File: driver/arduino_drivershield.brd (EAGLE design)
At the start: 59.7 x 54.3 mm, 24 parts, among them IC1 LB1973M, IC10 LB1973M, IC11 LB1973M, IC12 74HC14D, IC2 LB1973M, IC3 74HC14D, IC4 LB1973M, IC5 LB1973M, IC6 74HC14D, IC7 LB1973M, IC8 LB1973M, IC9 74HC14D, J1 J5MM, J2 J5MM, U1 ARDUINO_SHIELDLABEL

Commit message: testing routing
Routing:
- net @GND2: track 0.00 -> 157.7 mm, vias 0 -> 1
- net 5V: track 0.00 -> 111.5 mm, vias 0 -> 1
- net V+: track 0.00 -> 96.8 mm, vias 0 -> 2
- net GNDA: track 0.00 -> 92.5 mm, vias 0 -> 1
- net N$28: track 0.00 -> 90.5 mm
- net N$51: track 0.00 -> 74.4 mm, vias 0 -> 2
- net N$70: track 0.00 -> 32.1 mm
- net TX: track 0.00 -> 29.6 mm
- net RX: track 0.00 -> 29.0 mm
- net N$30: track 0.00 -> 25.0 mm, vias 0 -> 1
- net N$15: track 0.00 -> 23.9 mm, vias 0 -> 1
- net N$16: track 0.00 -> 23.9 mm, vias 0 -> 1
- net N$66: track 0.00 -> 23.5 mm, vias 0 -> 1
- net N$36: track 0.00 -> 22.2 mm, vias 0 -> 1
- net N$35: track 0.00 -> 21.8 mm
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
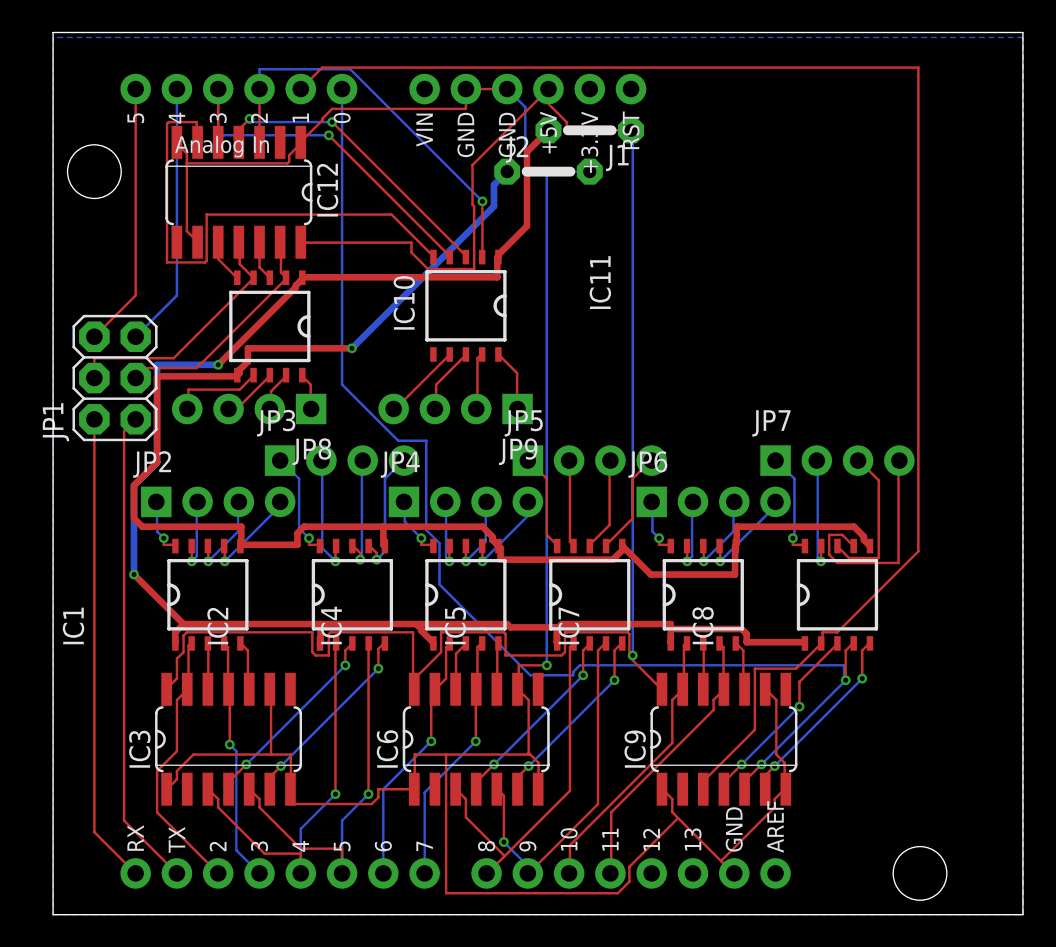
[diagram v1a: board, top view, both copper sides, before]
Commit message: bypass caps for all h-bridges
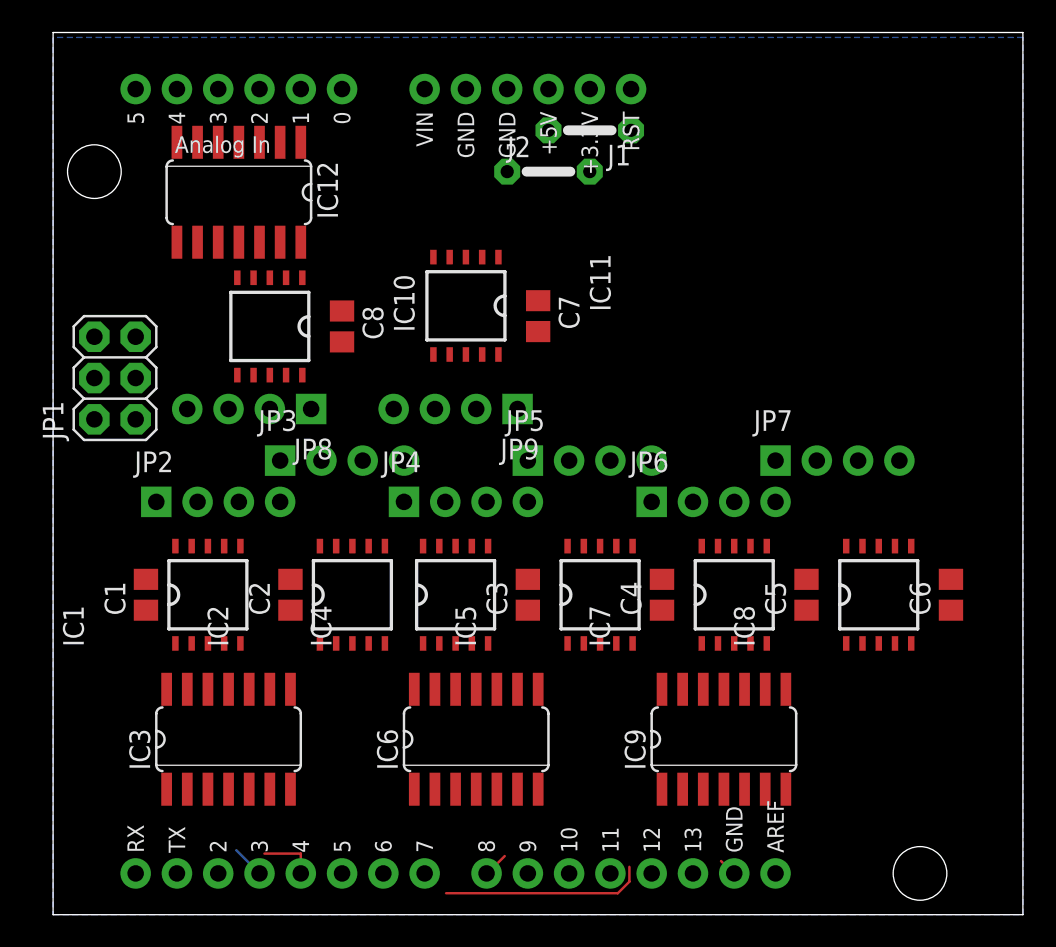
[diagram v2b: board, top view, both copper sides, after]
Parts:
- added C1, C2, C3, C4, C5, C6, C7, C8: (no value), rcl:C0805
- moved IC8 2.54 mm to (50.8, 19.7)
- moved IC7 1.90 mm to (41.9, 19.7)
- moved IC4 0.63 mm to (24.8, 19.7)
- moved IC5 0.63 mm to (33.7, 19.7)
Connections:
- net GNDA: now also C1.2, C2.2, C3.2, C4.2, C5.2, C6.2, C7.2, C8.2
- net V+: now also C1.1, C2.1, C3.1, C4.1, C5.1, C6.1, C7.1, C8.1
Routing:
- net @GND2: track 157.7 -> 13.6 mm, vias 1 -> 0
- net 5V: track 111.5 -> 0.00 mm, vias 1 -> 0
- net V+: track 96.8 -> 0.00 mm, vias 2 -> 0
- net GNDA: track 92.5 -> 0.00 mm, vias 1 -> 0
- net N$28: track 90.5 -> 0.00 mm
- net N$51: track 74.4 -> 0.00 mm, vias 2 -> 0
- net N$70: track 32.1 -> 0.00 mm
- net TX: track 29.6 -> 0.00 mm
- net RX: track 29.0 -> 0.00 mm
- net N$30: track 25.0 -> 0.00 mm, vias 1 -> 0
- net N$16: track 23.9 -> 0.00 mm, vias 1 -> 0
- net N$66: track 23.5 -> 0.00 mm, vias 1 -> 0
- net N$36: track 22.2 -> 0.61 mm, vias 1 -> 0
- net N$15: track 23.9 -> 3.45 mm, vias 1 -> 0
- net N$35: track 21.8 -> 1.56 mm
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
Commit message: the expiriment with the @signal names did not work out
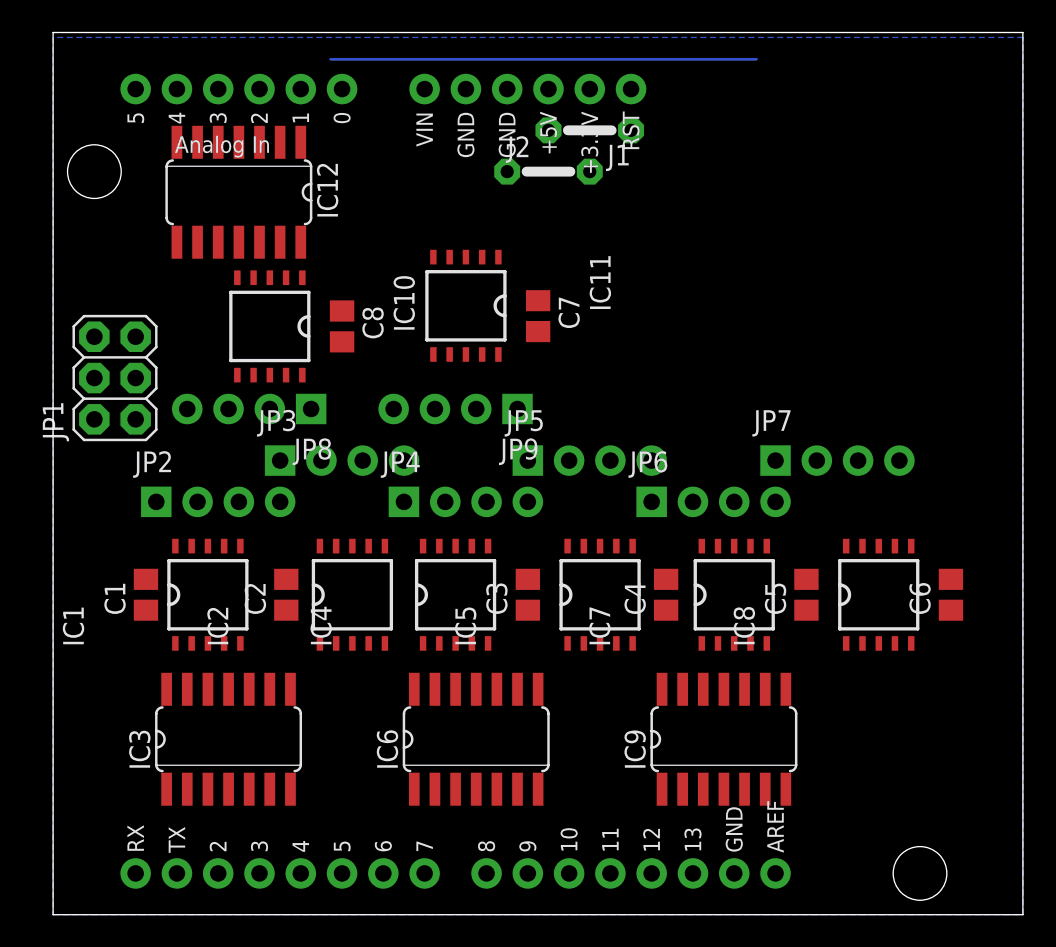
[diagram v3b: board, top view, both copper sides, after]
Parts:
- moved C2 0.25 mm to (14.4, 19.7)
- moved C4 0.25 mm to (37.7, 19.7)
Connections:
- removed net @GND3: IC11.6
- net GNDA: now also IC11.6
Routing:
- net N$28: track 0.00 -> 26.2 mm
- net @GND2: track 13.6 -> 0.00 mm
- net N$15: track 3.45 -> 0.00 mm
- net N$13: track 2.01 -> 0.00 mm
- net N$35: track 1.56 -> 0.00 mm
- net N$36: track 0.61 -> 0.00 mm

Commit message: the expiriment with the @signal names did not work out
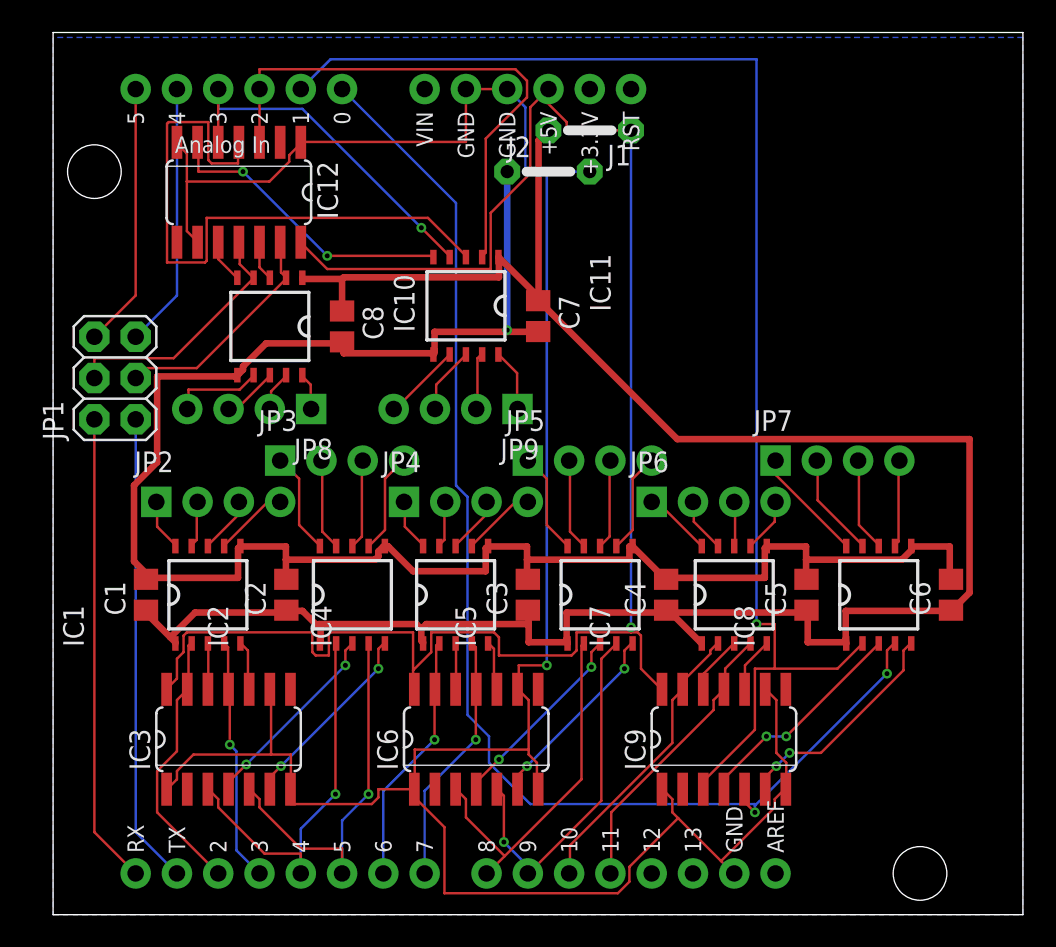
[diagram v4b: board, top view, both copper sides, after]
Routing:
- net @GND2: track 0.00 -> 158.4 mm, vias 0 -> 1
- net V+: track 0.00 -> 136.6 mm
- net GNDA: track 0.00 -> 116.1 mm, vias 0 -> 1
- net 5V: track 0.00 -> 109.4 mm, vias 0 -> 1
- net N$51: track 0.00 -> 78.4 mm, vias 0 -> 2
- net N$28: track 26.2 -> 83.4 mm, vias 0 -> 1
- net N$69: track 0.00 -> 38.8 mm
- net N$30: track 0.00 -> 33.2 mm
- net TX: track 0.00 -> 29.0 mm
- net RX: track 0.00 -> 29.0 mm
- net N$15: track 0.00 -> 23.9 mm, vias 0 -> 1
- net N$16: track 0.00 -> 23.9 mm, vias 0 -> 1
- net N$66: track 0.00 -> 22.5 mm, vias 0 -> 1
- net N$36: track 0.00 -> 22.4 mm, vias 0 -> 1
- net N$35: track 0.00 -> 22.0 mm
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
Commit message: the formar was SIGNAL@num...
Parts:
- removed J2: J5MM, jumper:05
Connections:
- net 5V renamed 5V@1
- removed net @GND2: IC12.1, IC12.7, IC12.9, IC3.1, IC3.7, IC3.9, IC6.1, IC6.7, IC6.9, IC9.1, IC9.7, IC9.9, J2.2, U1.GND@0, U1.GND@1, U1.GND@2
- removed net GNDA: C1.2, C2.2, C3.2, C4.2, C5.2, C6.2, C7.2, C8.2, IC1.6, IC10.6, IC11.6, IC2.6, IC4.6, IC5.6, IC7.6, IC8.6, J2.1
- new net GND@2: IC12.1, IC12.7, IC12.9, IC3.1, IC3.7, IC3.9, IC6.1, IC6.7, IC6.9, IC9.1, IC9.7, IC9.9, U1.GND@0, U1.GND@1, U1.GND@2
- new net GND@3: C1.2, C2.2, C3.2, C4.2, C5.2, C6.2, C7.2, C8.2, IC1.6, IC10.6, IC11.6, IC2.6, IC4.6, IC5.6, IC7.6, IC8.6
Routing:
- net @GND2: track 158.4 -> 0.00 mm, vias 1 -> 0
- net V+: track 136.6 -> 0.00 mm
- net GNDA: track 116.1 -> 0.00 mm, vias 1 -> 0
- net 5V@1: track 109.4 -> 0.00 mm, vias 1 -> 0
- net N$28: track 83.4 -> 0.00 mm, vias 1 -> 0
- net N$51: track 78.4 -> 0.00 mm, vias 2 -> 0
- net N$69: track 38.8 -> 0.00 mm
- net N$30: track 33.2 -> 0.00 mm
- net TX: track 29.0 -> 0.00 mm
- net RX: track 29.0 -> 0.00 mm
- net N$15: track 23.9 -> 0.00 mm, vias 1 -> 0
- net N$16: track 23.9 -> 0.00 mm, vias 1 -> 0
- net N$66: track 22.5 -> 0.00 mm, vias 1 -> 0
- net N$36: track 22.4 -> 0.00 mm, vias 1 -> 0
- net N$35: track 22.0 -> 0.00 mm
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- added copper zone on layer 16, net GND@2
- removed copper zone on layer 16, net @GND1

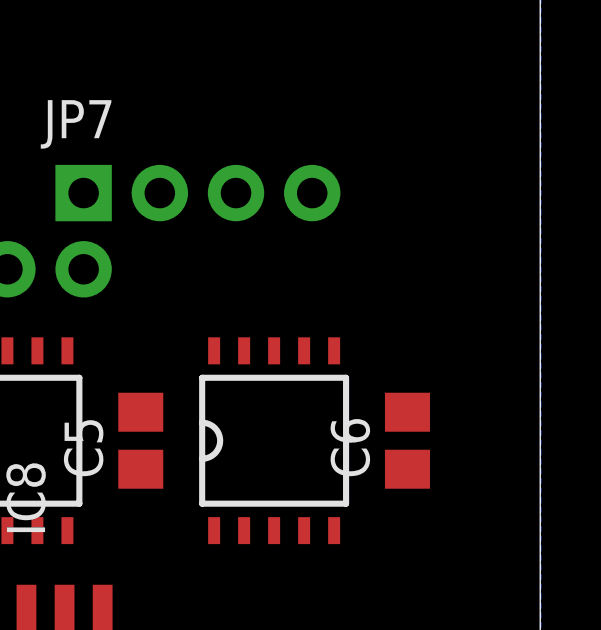
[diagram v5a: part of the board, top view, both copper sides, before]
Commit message: but it seems it only works in IC definitions :(
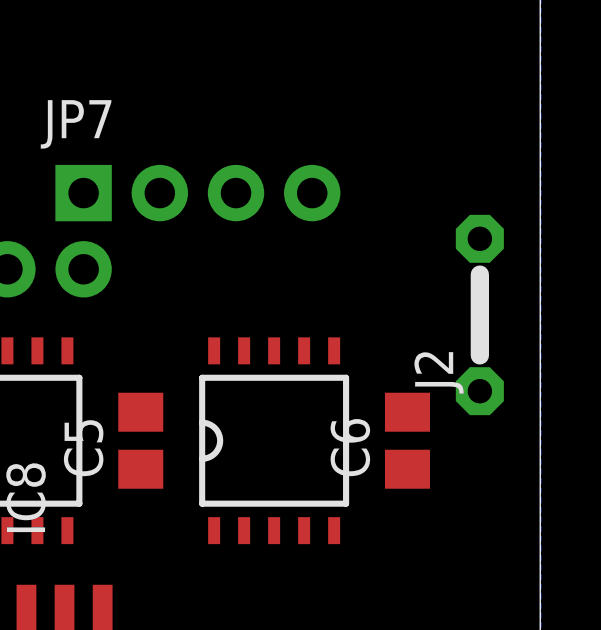
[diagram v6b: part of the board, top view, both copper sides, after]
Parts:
- added J2: J5MM, jumper:05
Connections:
- net GND@2: now also J2.2
- net GND@3: now also J2.1
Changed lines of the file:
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@@
 <element name="C7" library="rcl" package="C0805" value="" x="29.845" y="36.83" rot="R270"/>
 <element name="C8" library="rcl" package="C0805" value="" x="17.78" y="36.195" rot="R270"/>
+<element name="J2" library="jumper" package="05" value="J5MM" x="57.658" y="23.876" rot="R90"/>
 </elements>
 <signals>
@@
 <contactref element="IC11" pad="6"/>
 <contactref element="IC11" pad="6"/>
+<contactref element="J2" pad="1"/>
+<wire x1="55.245" y1="20.635" x2="57.658" y2="21.336" width="0" layer="19" extent="1-1"/>
 <wire x1="52.8" y1="22.681" x2="55.245" y2="20.635" width="0" layer="19" extent="1-1"/>
 <wire x1="46.355" y1="20.635" x2="52.8" y2="22.681" width="0" layer="19" extent="1-1"/>
@@
 <contactref element="IC12" pad="9"/>
 <contactref element="IC12" pad="1"/>
+<contactref element="J2" pad="2"/>
 <wire x1="7.62" y1="47.5234" x2="15.24" y2="47.5234" width="0" layer="19" extent="1-1"/>
 <wire x1="8.89" y1="41.3766" x2="7.62" y2="47.5234" width="0" layer="19" extent="1-1"/>

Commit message: so back top bridging with wires...
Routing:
- net V+: track 0.00 -> 139.6 mm
- net GND@2: track 0.00 -> 125.9 mm
- net 5V@1: track 0.00 -> 110.0 mm, vias 0 -> 1
- net GND@3: track 0.00 -> 108.7 mm
- net N$28: track 0.00 -> 69.6 mm, vias 0 -> 1
- net N$51: track 0.00 -> 68.7 mm, vias 0 -> 2
- net N$70: track 0.00 -> 32.1 mm
- net N$30: track 0.00 -> 29.6 mm
- net TX: track 0.00 -> 29.0 mm
- net RX: track 0.00 -> 29.0 mm
- net N$15: track 0.00 -> 23.9 mm, vias 0 -> 1
- net N$16: track 0.00 -> 23.9 mm, vias 0 -> 1
- net N$66: track 0.00 -> 22.5 mm, vias 0 -> 1
- net N$36: track 0.00 -> 22.4 mm, vias 0 -> 1
- net N$35: track 0.00 -> 22.0 mm
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
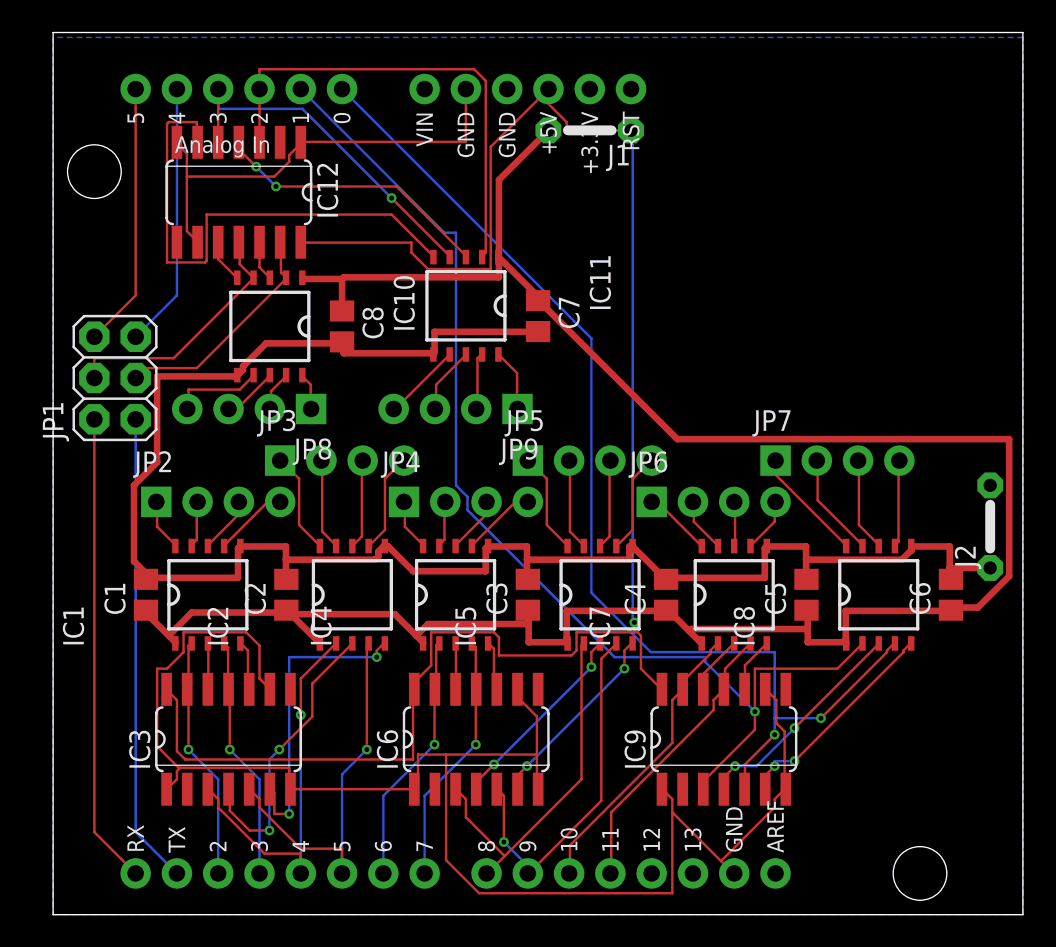
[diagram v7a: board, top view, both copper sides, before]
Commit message: add caps for the inverters too
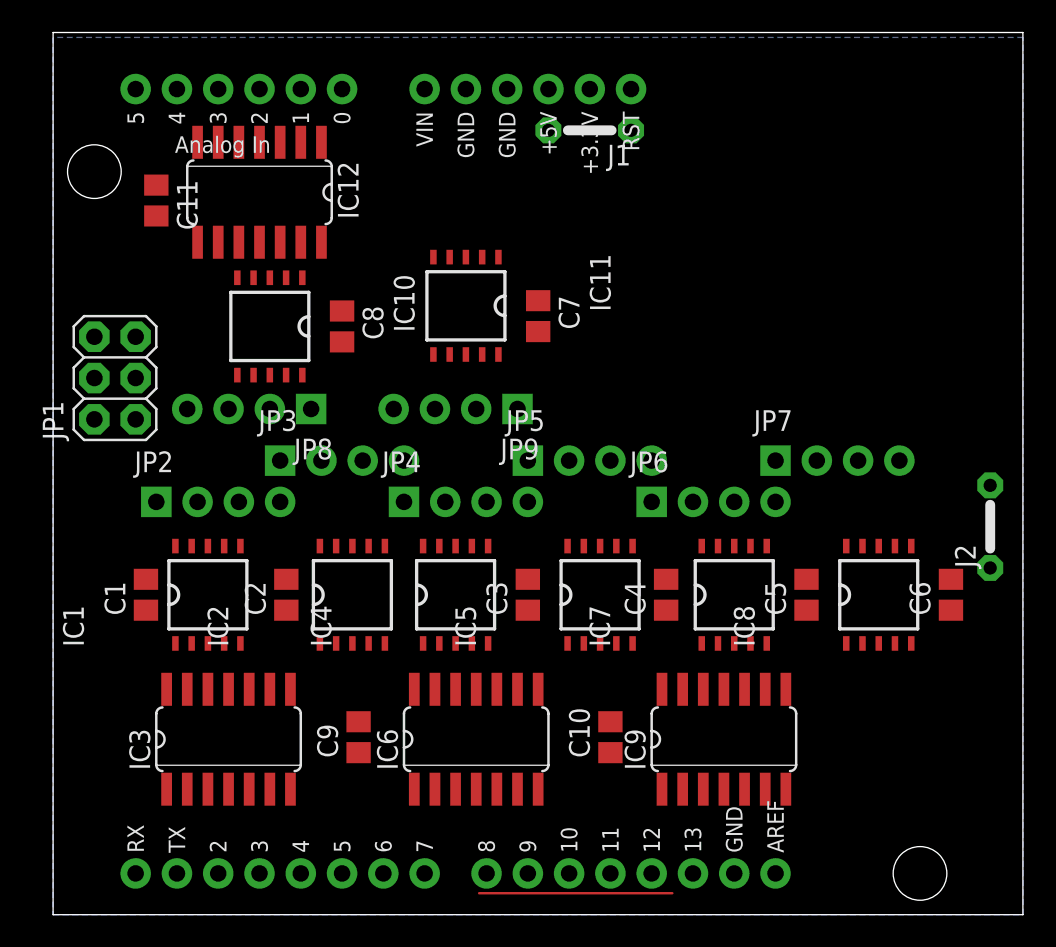
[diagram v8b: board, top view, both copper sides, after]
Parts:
- added C10, C11, C9: (no value), rcl:C0805
- moved IC12 1.27 mm to (12.7, 44.5)
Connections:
- new net 5V: C10.2, C11.2, C9.2, U1.5V
- net 5V@1: no longer U1.5V
- net GND@2: now also C10.1, C11.1, C9.1
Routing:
- net V+: track 139.6 -> 0.00 mm
- net GND@2: track 125.9 -> 11.9 mm
- net 5V@1: track 110.0 -> 0.00 mm, vias 1 -> 0
- net GND@3: track 108.7 -> 0.00 mm
- net N$28: track 69.6 -> 0.00 mm, vias 1 -> 0
- net N$51: track 68.7 -> 0.00 mm, vias 2 -> 0
- net N$70: track 32.1 -> 0.00 mm
- net N$30: track 29.6 -> 0.00 mm
- net TX: track 29.0 -> 0.00 mm
- net RX: track 29.0 -> 0.00 mm
- net N$15: track 23.9 -> 0.00 mm, vias 1 -> 0
- net N$16: track 23.9 -> 0.00 mm, vias 1 -> 0
- net N$66: track 22.5 -> 0.00 mm, vias 1 -> 0
- net N$36: track 22.4 -> 0.00 mm, vias 1 -> 0
- net N$35: track 22.0 -> 0.00 mm
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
